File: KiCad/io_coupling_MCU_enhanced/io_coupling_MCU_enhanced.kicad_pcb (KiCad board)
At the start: 4 copper layers, 72.8 x 82.1 mm, 76 parts, among them IC1 AP63205, IC2 AP2112K-3.3TRG1, J10 10PIN_HEADER, J2 Conn_Coaxial, J3 10PIN_HEADER, J4 10PIN_HEADER, J5 1987724, J6 1987724, J7 1987724, J8 1987724, J9 10PIN_HEADER, Q1 BSS138K-13/BSS159NH6327XTSA2, Q2 Si7469DP, Q3 BSS138K-13, Q4 BSS138K-13, Q5 BSS138K-13, Q6 RN2903, Q7 RN2903, U1 HOLE, U2 HOLE, U3 HOLE, U4 HOLE, U5 HOLE

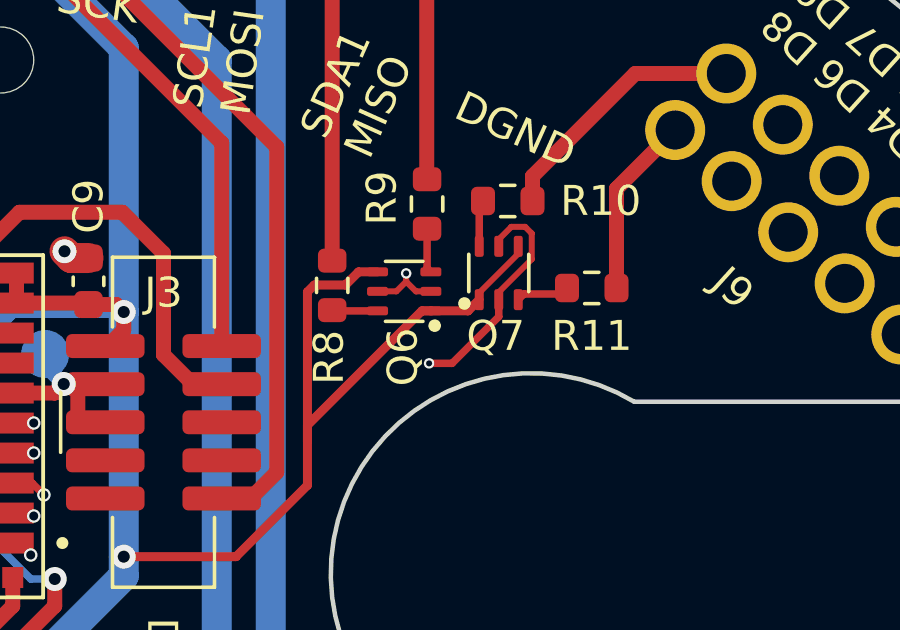
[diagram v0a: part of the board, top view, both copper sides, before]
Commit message: removed tiny vias, removed legacy backup files, removed legacy gerber files
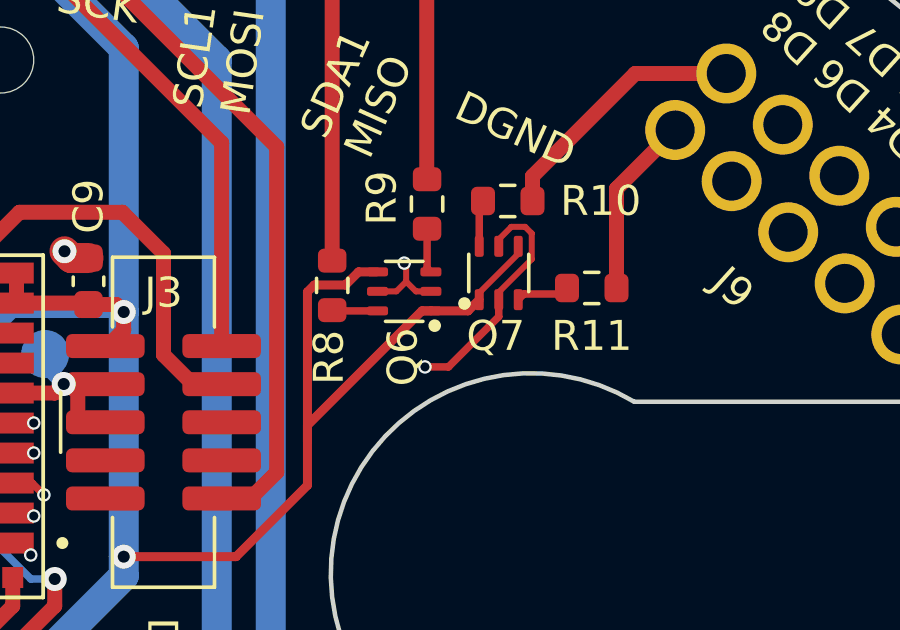
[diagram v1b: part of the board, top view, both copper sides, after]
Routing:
- net /EN_I2C1: track 26.2 -> 26.9 mm
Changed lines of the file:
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@@
   (segment (start 26.068208 -34.731792) (end 26.068208 -32.645734) (width 0.25) (layer "In2.Cu") (net 61))
   (segment (start 24.9 -35.9) (end 26.068208 -34.731792) (width 0.25) (layer "In2.Cu") (net 61))
+  (segment (start 13.513924 -27.966076) (end 13.513924 -27.413924) (width 0.2) (layer "F.Cu") (net 67))
   (segment (start 13.1875 -27.0875) (end 12.5595 -27.0875) (width 0.2) (layer "F.Cu") (net 67))
   (segment (start 13.840348 -27.0875) (end 14.3375 -27.0875) (width 0.2) (layer "F.Cu") (net 67))
   (segment (start -3.05 -20.45) (end -3 -20.5) (width 0.25) (layer "F.Cu") (net 67))
-  (segment (start 13.513924 -27.686076) (end 13.513924 -27.413924) (width 0.2) (layer "F.Cu") (net 67))
+  (segment (start 13.45 -28.03) (end 13.513924 -27.966076) (width 0.2) (layer "F.Cu") (net 67))
   (segment (start 13.513924 -27.413924) (end 13.840348 -27.0875) (width 0.2) (layer "F.Cu") (net 67))
   (segment (start -3.05 -20.149) (end -3.05 -20.45) (width 0.25) (layer "F.Cu") (net 67))
   (segment (start 13.513924 -27.413924) (end 13.1875 -27.0875) (width 0.2) (layer "F.Cu") (net 67))
   (via (at -3 -20.5) (size 0.45) (drill 0.3) (layers "F.Cu" "B.Cu") (net 67))
-  (via (at 13.513924 -27.686076) (size 0.35) (drill 0.2) (layers "F.Cu" "B.Cu") (free) (net 67))
+  (via (at 13.45 -28.03) (size 0.45) (drill 0.3) (layers "F.Cu" "B.Cu") (free) (net 67))
+  (segment (start 0.625 -16.775) (end -0.780853 -18.180853) (width 0.25) (layer "In2.Cu") (net 67))
+  (segment (start 3.65594 -16.775) (end 0.625 -16.775) (width 0.25) (layer "In2.Cu") (net 67))
   (segment (start -0.780853 -18.680853) (end -2.15 -20.05) (width 0.25) (layer "In2.Cu") (net 67))
   (segment (start -0.780853 -18.180853) (end -0.780853 -18.680853) (width 0.25) (layer "In2.Cu") (net 67))
+  (segment (start 13.45 -28.03) (end 4.925 -19.505) (width 0.25) (layer "In2.Cu") (net 67))
+  (segment (start 4.925 -19.505) (end 4.925 -18.04406) (width 0.25) (layer "In2.Cu") (net 67))
   (segment (start -2.15 -20.05) (end -2.55 -20.05) (width 0.25) (layer "In2.Cu") (net 67))
-  (segment (start 3.65594 -16.775) (end 0.625 -16.775) (width 0.25) (layer "In2.Cu") (net 67))
+  (segment (start -2.55 -20.05) (end -3 -20.5) (width 0.25) (layer "In2.Cu") (net 67))
   (segment (start 4.925 -18.04406) (end 3.65594 -16.775) (width 0.25) (layer "In2.Cu") (net 67))
-  (segment (start 0.625 -16.775) (end -0.780853 -18.180853) (width 0.25) (layer "In2.Cu") (net 67))
-  (segment (start 4.925 -19.025001) (end 4.925 -18.04406) (width 0.25) (layer "In2.Cu") (net 67))
-  (segment (start 13.513924 -27.613924) (end 4.925 -19.025001) (width 0.25) (layer "In2.Cu") (net 67))
-  (segment (start -2.55 -20.05) (end -3 -20.5) (width 0.25) (layer "In2.Cu") (net 67))
-  (segment (start 13.513924 -27.686076) (end 13.513924 -27.613924) (width 0.25) (layer "In2.Cu") (net 67))
   (segment (start 14.211 -27.864) (end 14.3375 -27.7375) (width 0.25) (layer "F.Cu") (net 68))
   (segment (start 14.211 -29.175) (end 14.211 -27.864) (width 0.25) (layer "F.Cu") (net 68))
@@
   (segment (start 11.0735 -26.4375) (end 11.0485 -26.4625) (width 0.25) (layer "F.Cu") (net 69))
   (segment (start 16.6 -26.2436) (end 16.6 -26.811) (width 0.25) (layer "F.Cu") (net 70))
+  (segment (start 14.14 -24.57) (end 14.9264 -24.57) (width 0.25) (layer "F.Cu") (net 70))
   (segment (start 16.6 -27.05867) (end 17.7 -28.15867) (width 0.2) (layer "F.Cu") (net 70))
   (segment (start 17.7 -29.01933) (end 17.48033 -29.239) (width 0.2) (layer "F.Cu") (net 70))
@@
   (segment (start 17.48033 -29.239) (end 17.01967 -29.239) (width 0.2) (layer "F.Cu") (net 70))
   (segment (start 16.6 -28.81933) (end 16.6 -28.589) (width 0.2) (layer "F.Cu") (net 70))
-  (segment (start 15.0444 -24.688) (end 16.6 -26.2436) (width 0.25) (layer "F.Cu") (net 70))
   (segment (start 17.7 -28.15867) (end 17.7 -29.01933) (width 0.2) (layer "F.Cu") (net 70))
+  (segment (start 14.9264 -24.57) (end 16.6 -26.2436) (width 0.25) (layer "F.Cu") (net 70))
   (segment (start -6.35 -20.149) (end -6.35 -20.15) (width 0.25) (layer "F.Cu") (net 70))
-  (segment (start 14.2782 -24.688) (end 15.0444 -24.688) (width 0.25) (layer "F.Cu") (net 70))
   (via (at -6.424502 -20.374498) (size 0.45) (drill 0.3) (layers "F.Cu" "B.Cu") (net 70))
-  (via (at 14.2782 -24.688) (size 0.35) (drill 0.2) (layers "F.Cu" "B.Cu") (net 70))
-  (segment (start -5.77 -18.94) (end -5.77 -17.833604) (width 0.25) (layer "In2.Cu") (net 70))
-  (segment (start -6.424502 -19.594502) (end -5.77 -18.94) (width 0.25) (layer "In2.Cu") (net 70))
-  (segment (start 7.125 -17.575) (end 14.238 -24.688) (width 0.25) (layer "In2.Cu") (net 70))
-  (segment (start 3.933631 -13.8) (end 7.125 -16.991369) (width 0.25) (layer "In2.Cu") (net 70))
-  (segment (start -1.736396 -13.8) (end 3.933631 -13.8) (width 0.25) (layer "In2.Cu") (net 70))
-  (segment (start 7.125 -16.991369) (end 7.125 -17.575) (width 0.25) (layer "In2.Cu") (net 70))
-  (segment (start -5.77 -17.833604) (end -1.736396 -13.8) (width 0.25) (layer "In2.Cu") (net 70))
-  (segment (start -6.424502 -20.374498) (end -6.424502 -19.594502) (width 0.25) (layer "In2.Cu") (net 70))
-  (segment (start 14.238 -24.688) (end 14.2782 -24.688) (width 0.25) (layer "In2.Cu") (net 70))
+  (via (at 14.14 -24.57) (size 0.45) (drill 0.3) (layers "F.Cu" "B.Cu") (net 70))
+  (segment (start -6.424502 -19.594502) (end -6.424502 -20.374498) (width 0.25) (layer "In2.Cu") (net 70))
+  (segment (start 3.933631 -13.8) (end -1.736396 -13.8) (width 0.25) (layer "In2.Cu") (net 70))
+  (segment (start -1.736396 -13.8) (end -5.77 -17.833604) (width 0.25) (layer "In2.Cu") (net 70))
+  (segment (start -5.77 -18.94) (end -6.424502 -19.594502) (width 0.25) (layer "In2.Cu") (net 70))
+  (segment (start 14.12 -24.57) (end 7.125 -17.575) (width 0.25) (layer "In2.Cu") (net 70))
+  (segment (start 14.14 -24.57) (end 14.12 -24.57) (width 0.25) (layer "In2.Cu") (net 70))
+  (segment (start -5.77 -17.833604) (end -5.77 -18.94) (width 0.25) (layer "In2.Cu") (net 70))
+  (segment (start 7.125 -16.991369) (end 3.933631 -13.8) (width 0.25) (layer "In2.Cu") (net 70))
+  (segment (start 7.125 -17.575) (end 7.125 -16.991369) (width 0.25) (layer "In2.Cu") (net 70))
   (segment (start 17.25 -26.811) (end 17.439 -27) (width 0.25) (layer "F.Cu") (net 71))
   (segment (start 18.675 -27) (end 18.875 -27.2) (width 0.25) (layer "F.Cu") (net 71))

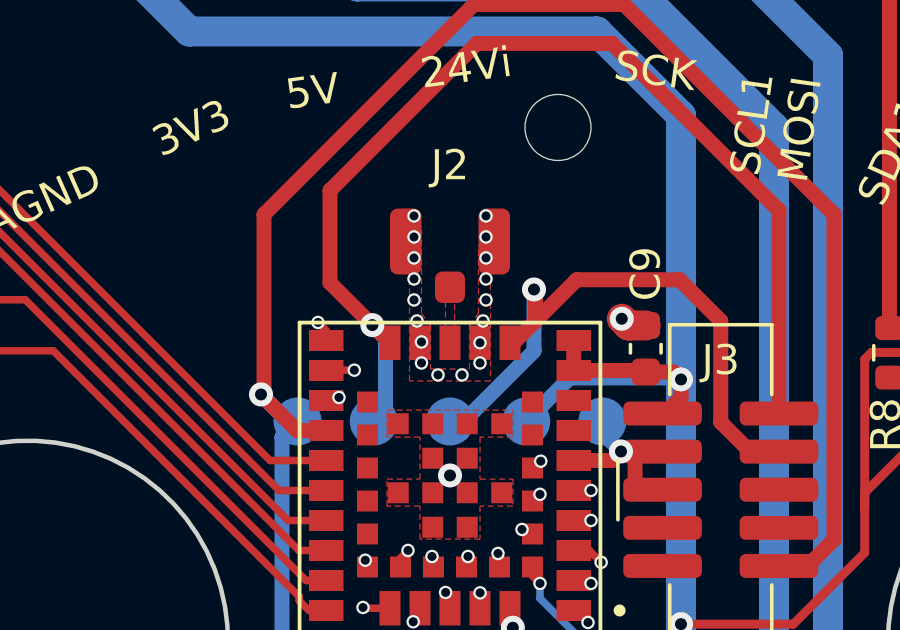
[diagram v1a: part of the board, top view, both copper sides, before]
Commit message: fixed width of antenna trace
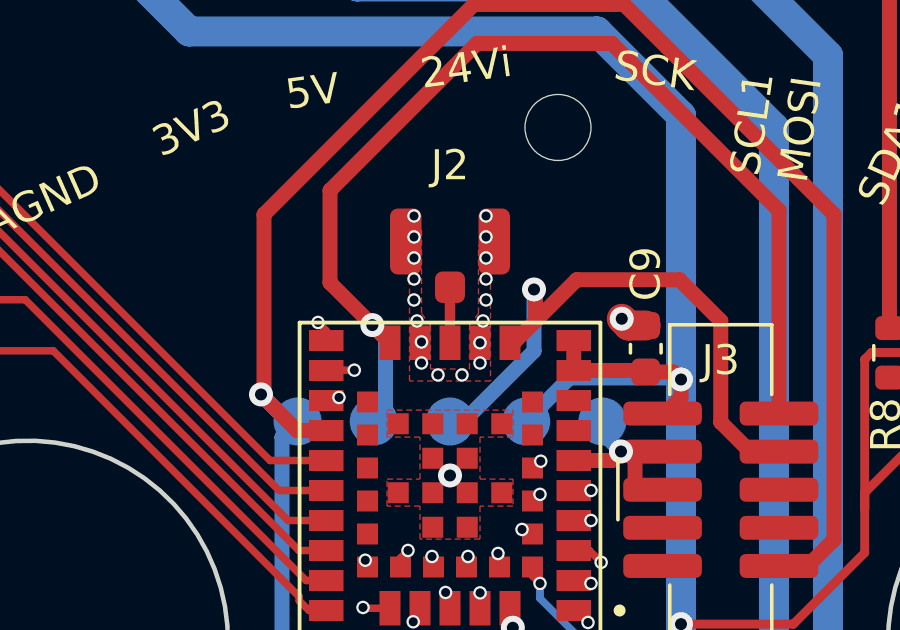
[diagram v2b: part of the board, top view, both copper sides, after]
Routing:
- net /ANT: track 0.00 -> 1.85 mm
- removed copper zone on F.Cu, net /ANT
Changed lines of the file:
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@@
   (segment (start -30.862 -2.7) (end -30.448 -2.7) (width 0.5) (layer "F.Cu") (net 40))
   (segment (start -24.558 -8.59) (end -21.952 -8.59) (width 0.5) (layer "F.Cu") (net 40))
+  (segment (start -3.6 -27.624) (end -3.6 -29.4738) (width 0.35) (layer "F.Cu") (net 41))
   (segment (start 0 23) (end 0 20.46) (width 1) (layer "B.Cu") (net 43))
   (segment (start 0 20.46) (end 0 19) (width 1) (layer "B.Cu") (net 43))
@@
   (segment (start -7.725 -21.699) (end -8.999 -21.699) (width 0.25) (layer "F.Cu") (net 80))
   (segment (start -8.999 -21.699) (end -19.765877 -32.465877) (width 0.25) (layer "F.Cu") (net 80))
-  (zone (net 41) (net_name "/ANT") (layer "F.Cu") (hatch full 0.5)
-    (priority 2)
-    (connect_pads yes (clearance 0))
-    (min_thickness 0.25) (filled_areas_thickness no)
-    (fill yes (thermal_gap 0.5) (thermal_bridge_width 0.5))
-    (polygon
-      (pts
-        (xy -3.75 -27.8288)
-        (xy -3.75 -29.2288)
-        (xy -3.45 -29.2288)
-        (xy -3.45 -27.8288)
-      )
-    )
-  )
   (zone (net 1) (net_name "GND") (layer "F.Cu") (hatch edge 0.5)
     (priority 3)

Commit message: reworked annotations, removed kicad backup files
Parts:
- R2: renamed from R4; value 150 -> 325
- R4: renamed from R6; value 150 -> 750
- R6: renamed from R7; value 150 -> 325
- renumbered B2 to B1, C2 to C1, C12 to C10, C9 to C11, C1 to C12, C3 to C2, C8 to C3, C7 to C4, C10 to C5, C11 to C6, C4 to C7, C5 to C8, C6 to C9, D3 to D1, D6 to D2, D5 to D3, D1 to D4, D2 to D5, J4 to J10, J8 to J3, J7 to J4, J6 to J5, J5 to J6, J9 to J7, J10 to J8, J3 to J9, Q3 to Q1, Q6 to Q2, Q4 to Q3, Q5 to Q4, Q7 to Q5, Q1 to Q6, Q2 to Q7, R5 to R1, R2 to R10, R3 to R11, R8 to R3, R9 to R5, R10 to R7, R11 to R8, R1 to R9
